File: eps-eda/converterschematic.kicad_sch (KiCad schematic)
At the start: 24 parts, among them U1 TPS61022RWUR, U2 TPS61022RWUR, U3 INA3221AIRGVR

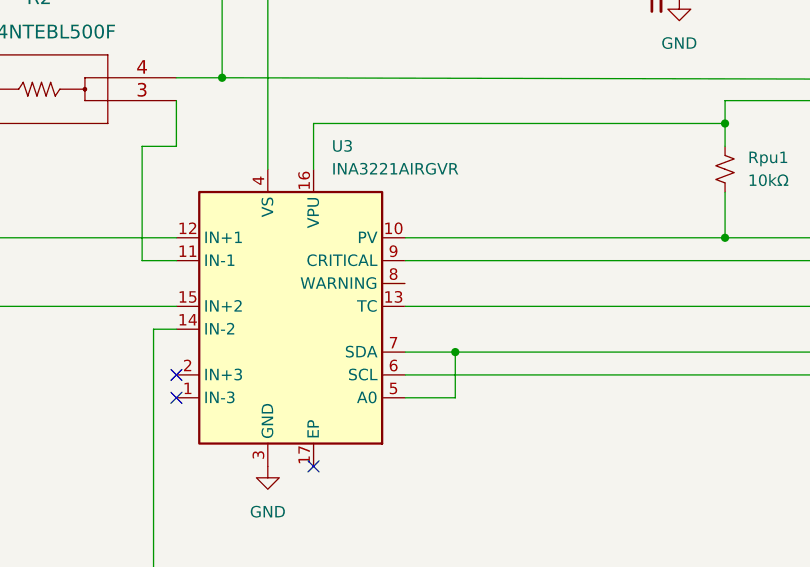
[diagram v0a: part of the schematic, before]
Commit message: EPS V0.2
Adjusted placement of resistors R19 through R23, and capacitor C18. For mounting purposes. Most DRC errors have now been cleared.
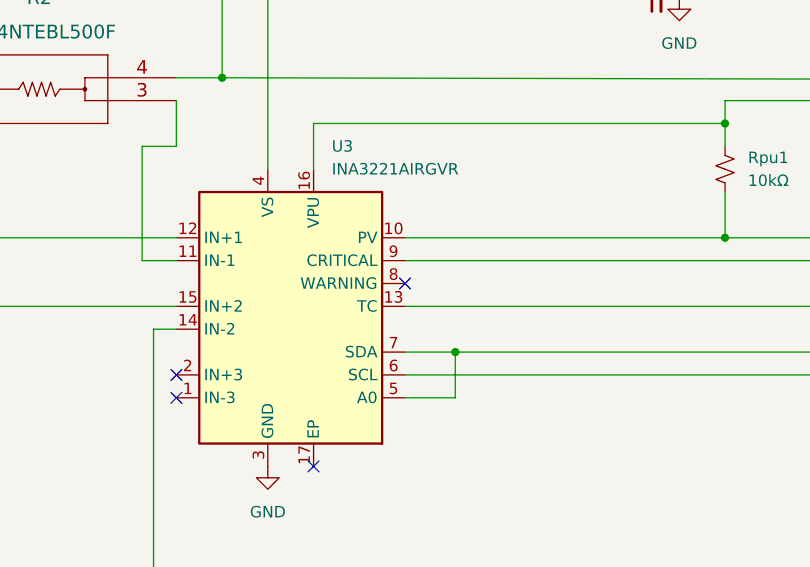
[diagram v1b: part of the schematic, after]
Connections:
- no-connect marks 3 -> 4
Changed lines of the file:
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@@
   (no_connect (at 151.892 82.804))
   (no_connect (at 151.892 80.264))
+  (no_connect (at 177.292 70.104))
   (no_connect (at 167.132 90.424))
   (wire (pts (xy 89.408 114.808) (xy 92.964 114.808))

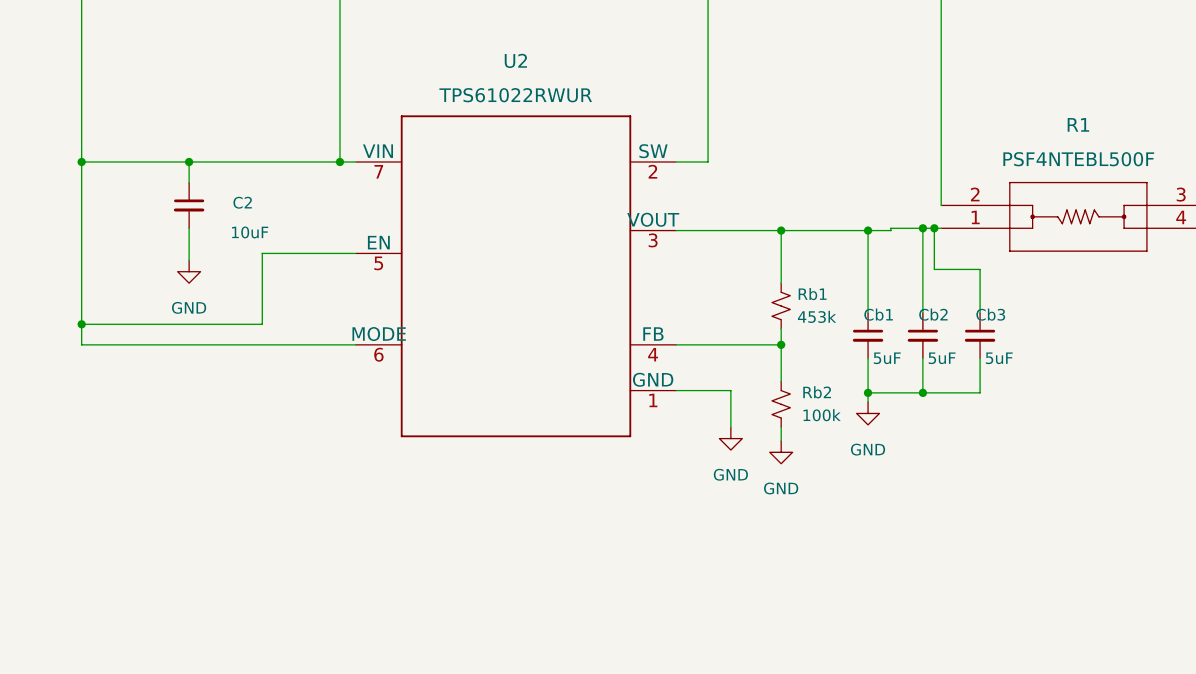
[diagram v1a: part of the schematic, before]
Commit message: EPS V0.2 quick update
added schottyky diode before 3.3V boost converter
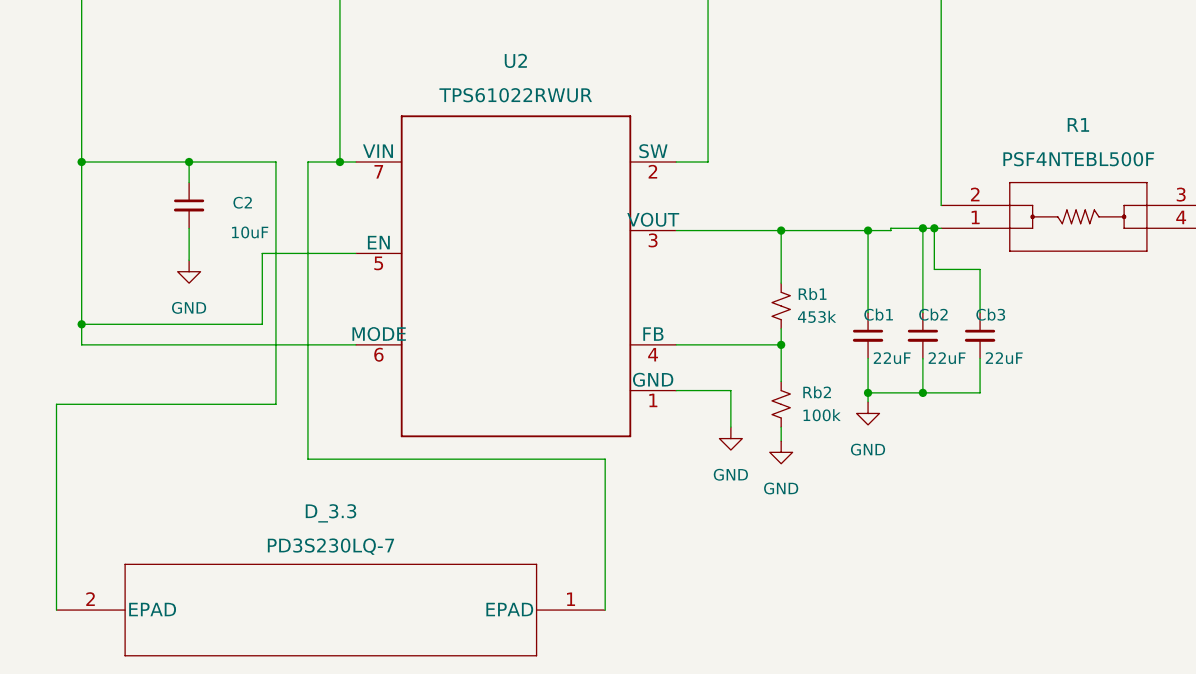
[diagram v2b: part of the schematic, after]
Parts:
- added D_3.3: PD3S230LQ-7, footprints3:PD3S230LQ-7, symbol 2022-04-23_02-59-39:PD3S230LQ-7
- Cb1, Cb2, Cb3: value 5uF -> 22uF
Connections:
- net Vin: now also D_3.3.2 (EPAD); no longer L3.2, U2.7 (VIN)
- new net: D_3.3.1 (EPAD), L3.2, U2.7 (VIN)
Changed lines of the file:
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@@
   (junction (at 114.808 59.182) (diameter 0) (color 0 0 0 0)
   )
+  (junction (at 52.07 114.808) (diameter 0) (color 0 0 0 0)
+  )
   (junction (at 100.838 59.182) (diameter 0) (color 0 0 0 0)
   )
@@
   (junction (at 109.982 76.454) (diameter 0) (color 0 0 0 0)
   )
+  (junction (at 118.11 122.174) (diameter 0) (color 0 0 0 0)
+  )
+  (junction (at 202.692 33.274) (diameter 0) (color 0 0 0 0)
+  )
+  (junction (at 156.972 47.244) (diameter 0) (color 0 0 0 0)
+  )
+  (junction (at 226.822 67.564) (diameter 0) (color 0 0 0 0)
+  )
+  (junction (at 113.03 59.182) (diameter 0) (color 0 0 0 0)
+  )
+  (junction (at 109.982 59.182) (diameter 0) (color 0 0 0 0)
+  )
+  (junction (at 182.88 77.724) (diameter 0) (color 0 0 0 0)
+  )
+  (junction (at 53.594 61.722) (diameter 0) (color 0 0 0 0)
+  )
+  (junction (at 110.744 122.428) (diameter 0) (color 0 0 0 0)
+  )
   (junction (at 35.306 114.808) (diameter 0) (color 0 0 0 0)
   )
-  (junction (at 118.11 122.174) (diameter 0) (color 0 0 0 0)
-  )
-  (junction (at 202.692 33.274) (diameter 0) (color 0 0 0 0)
-  )
-  (junction (at 156.972 47.244) (diameter 0) (color 0 0 0 0)
-  )
-  (junction (at 226.822 67.564) (diameter 0) (color 0 0 0 0)
-  )
-  (junction (at 113.03 59.182) (diameter 0) (color 0 0 0 0)
-  )
-  (junction (at 109.982 59.182) (diameter 0) (color 0 0 0 0)
-  )
-  (junction (at 182.88 77.724) (diameter 0) (color 0 0 0 0)
-  )
-  (junction (at 53.594 61.722) (diameter 0) (color 0 0 0 0)
-  )
-  (junction (at 110.744 122.428) (diameter 0) (color 0 0 0 0)
-  )
   (junction (at 114.808 76.454) (diameter 0) (color 0 0 0 0)
   )
@@
   )
   (junction (at 226.822 49.784) (diameter 0) (color 0 0 0 0)
-  )
-  (junction (at 52.07 114.808) (diameter 0) (color 0 0 0 0)
   )
   (junction (at 235.712 49.784) (diameter 0) (color 0 0 0 0)
@@
     (stroke (width 0) (type default) (color 0 0 0 0))
   )
+  (wire (pts (xy 44.958 114.808) (xy 35.306 114.808))
+    (stroke (width 0) (type default) (color 0 0 0 0))
+  )
   (wire (pts (xy 212.852 49.784) (xy 226.822 49.784))
     (stroke (width 0) (type default) (color 0 0 0 0))
@@
     (stroke (width 0) (type default) (color 0 0 0 0))
   )
+  (wire (pts (xy 20.574 164.592) (xy 20.574 141.732))
+    (stroke (width 0) (type default) (color 0 0 0 0))
+  )
   (wire (pts (xy 182.88 77.724) (xy 263.652 77.724))
     (stroke (width 0) (type default) (color 0 0 0 0))
@@
     (stroke (width 0) (type default) (color 0 0 0 0))
   )
+  (wire (pts (xy 20.574 141.732) (xy 44.958 141.732))
+    (stroke (width 0) (type default) (color 0 0 0 0))
+  )
   (wire (pts (xy 212.852 59.944) (xy 212.852 65.024))
     (stroke (width 0) (type default) (color 0 0 0 0))
@@
     (stroke (width 0) (type default) (color 0 0 0 0))
   )
+  (wire (pts (xy 44.958 141.732) (xy 44.958 114.808))
+    (stroke (width 0) (type default) (color 0 0 0 0))
+  )
   (wire (pts (xy 51.816 31.75) (xy 51.816 51.562))
     (stroke (width 0) (type default) (color 0 0 0 0))
@@
     (stroke (width 0) (type default) (color 0 0 0 0))
   )
+  (wire (pts (xy 81.534 164.592) (xy 81.534 147.828))
+    (stroke (width 0) (type default) (color 0 0 0 0))
+  )
   (wire (pts (xy 89.154 51.562) (xy 92.71 51.562))
     (stroke (width 0) (type default) (color 0 0 0 0))
@@
     (stroke (width 0) (type default) (color 0 0 0 0))
   )
-  (wire (pts (xy 52.07 114.808) (xy 35.306 114.808))
-    (stroke (width 0) (type default) (color 0 0 0 0))
-  )
   (wire (pts (xy 113.03 47.244) (xy 121.412 47.244))
     (stroke (width 0) (type default) (color 0 0 0 0))
   )
+  (wire (pts (xy 48.514 147.828) (xy 48.514 114.808))
+    (stroke (width 0) (type default) (color 0 0 0 0))
+  )
+  (wire (pts (xy 81.534 147.828) (xy 48.514 147.828))
+    (stroke (width 0) (type default) (color 0 0 0 0))
+  )
   (wire (pts (xy 23.368 18.542) (xy 23.368 51.562))
     (stroke (width 0) (type default) (color 0 0 0 0))
@@
   )
   (wire (pts (xy 114.808 71.628) (xy 114.808 76.454))
+    (stroke (width 0) (type default) (color 0 0 0 0))
+  )
+  (wire (pts (xy 48.514 114.808) (xy 52.07 114.808))
     (stroke (width 0) (type default) (color 0 0 0 0))
   )
@@
       (effects (font (size 1.27 1.27)) (justify left))
     )
-    (property "Value" "5uF" (id 1) (at 111.252 136.652 0)
+    (property "Value" "22uF" (id 1) (at 111.252 136.652 0)
       (effects (font (size 1.27 1.27)) (justify left))
     )
@@
     )
     (property "Datasheet" "" (id 3) (at 63.246 94.996 0)
+      (effects (font (size 1.524 1.524)))
+    )
+    (pin "1")
+    (pin "2")
+  )
+  (symbol (lib_id "2022-04-23_02-59-39:PD3S230LQ-7") (at 81.534 164.592 180) (unit 1)
+    (in_bom yes) (on_board yes) (fields_autoplaced)
+    (property "Reference" "D_3.3" (id 0) (at 51.054 153.67 0)
+      (effects (font (size 1.524 1.524)))
+    )
+    (property "Value" "PD3S230LQ-7" (id 1) (at 51.054 157.48 0)
+      (effects (font (size 1.524 1.524)))
+    )
+    (property "Footprint" "footprints3:PD3S230LQ-7" (id 2) (at 51.054 170.688 0)
+      (effects (font (size 1.524 1.524)) hide)
+    )
+    (property "Datasheet" "" (id 3) (at 81.534 164.592 0)
       (effects (font (size 1.524 1.524)))
     )
@@
       (effects (font (size 1.27 1.27)) (justify left))
     )
-    (property "Value" "5uF" (id 1) (at 117.348 136.652 0)
+    (property "Value" "22uF" (id 1) (at 117.348 136.652 0)
       (effects (font (size 1.27 1.27)) (justify left))
     )
@@
       (effects (font (size 1.27 1.27)) (justify left))
     )
-    (property "Value" "5uF" (id 1) (at 123.698 136.652 0)
-      (effects (font (size 1.27 1.27)) (justify left))
-    )
+    (property "Value" "22uF" (id 1) (at 123.698 136.652 0)
+      (effects (font (size 1.27 1.27)) (justify left))
+    )

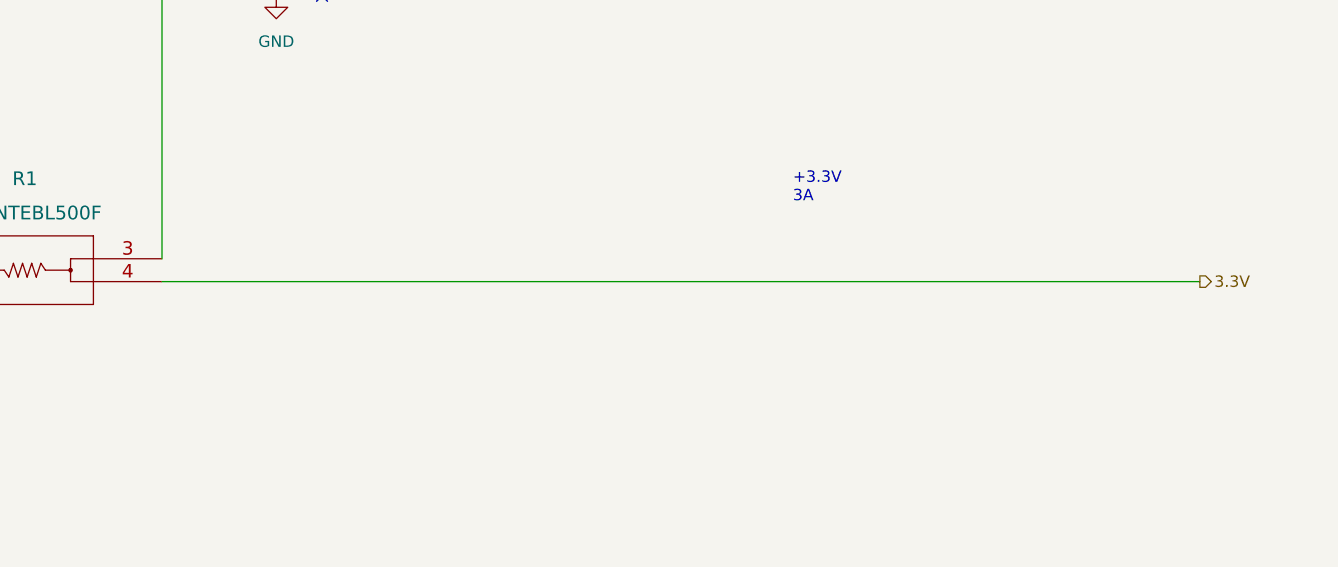
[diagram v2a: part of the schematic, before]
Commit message: EPS V0.3
Added over voltage protection system for the 3.3V rail.
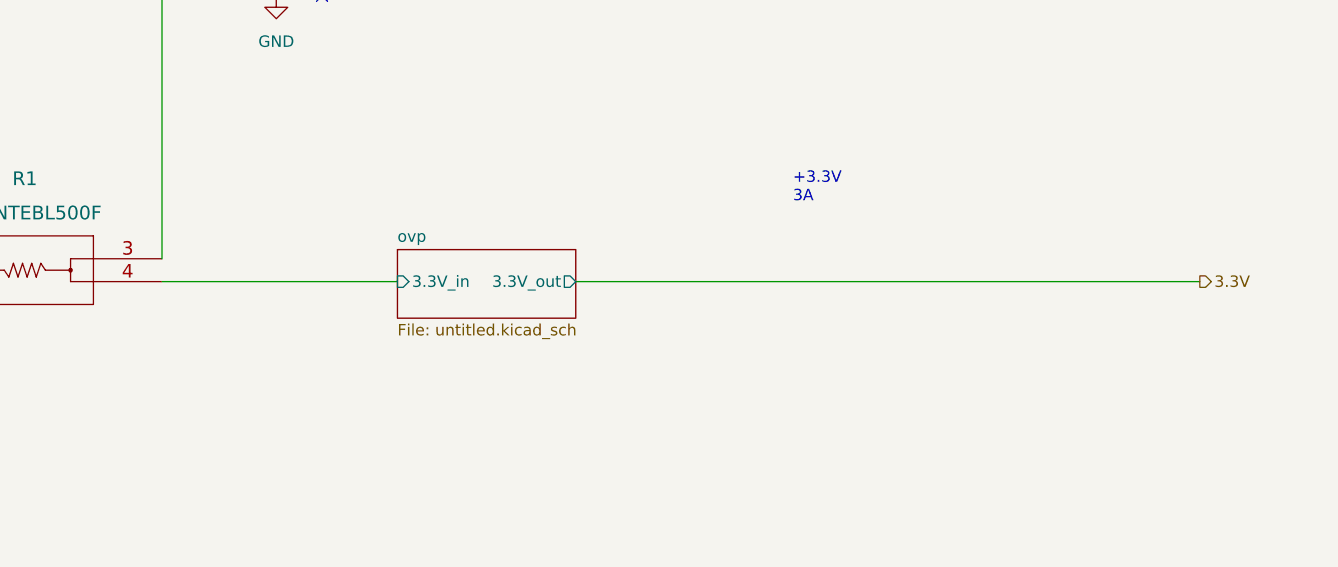
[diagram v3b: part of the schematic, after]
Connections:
- net 3.3V: no longer R1.4
- new net ovp/3.3V_in: R1.4
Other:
- added sheet ovp (untitled.kicad_sch)
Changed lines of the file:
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@@
+    (stroke (width 0) (type default) (color 0 0 0 0))
+  )
+  (wire (pts (xy 149.352 122.174) (xy 175.514 122.174))
     (stroke (width 0) (type default) (color 0 0 0 0))
   )
@@
     (stroke (width 0) (type default) (color 0 0 0 0))
   )
+  (wire (pts (xy 195.326 122.174) (xy 264.668 122.174))
+    (stroke (width 0) (type default) (color 0 0 0 0))
+  )
   (wire (pts (xy 92.964 114.808) (xy 92.964 94.996))
     (stroke (width 0) (type default) (color 0 0 0 0))
@@
   )
   (wire (pts (xy 53.848 124.968) (xy 43.434 124.968))
-    (stroke (width 0) (type default) (color 0 0 0 0))
-  )
-  (wire (pts (xy 149.352 122.174) (xy 264.668 122.174))
     (stroke (width 0) (type default) (color 0 0 0 0))
   )
@@
     (pin "2")
   )
+  (sheet (at 175.514 118.618) (size 19.812 7.62) (fields_autoplaced)
+    (stroke (width 0.1524) (type solid) (color 0 0 0 0))
+    (fill (color 0 0 0 0.0000))
+    (property "Sheet name" "ovp" (id 0) (at 175.514 117.9064 0)
+      (effects (font (size 1.27 1.27)) (justify left bottom))
+    )
+    (property "Sheet file" "untitled.kicad_sch" (id 1) (at 175.514 126.8226 0)
+      (effects (font (size 1.27 1.27)) (justify left top))
+    )
+    (pin "3.3V_in" input (at 175.514 122.174 180)
+      (effects (font (size 1.27 1.27)) (justify left))
+    )
+    (pin "3.3V_out" output (at 195.326 122.174 0)
+      (effects (font (size 1.27 1.27)) (justify right))
+    )
+  )
   (sheet_instances
